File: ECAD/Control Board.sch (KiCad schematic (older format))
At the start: 74 parts, among them J3 Thermocouple, J4 SD_Card, J5 PWR/Heat, J6 FAN, J7 UPDI, Q1 IPD50N06S4L08, Q2 IPD50N06S4L08, SW1 Reflow, SW2 Stop, SW3 Set temp mode, U1 ATtiny1614-SS, U2 LD1086DT33, U3 AD8497, U4 HT16K33, U5 LM2575HVS-ADJ

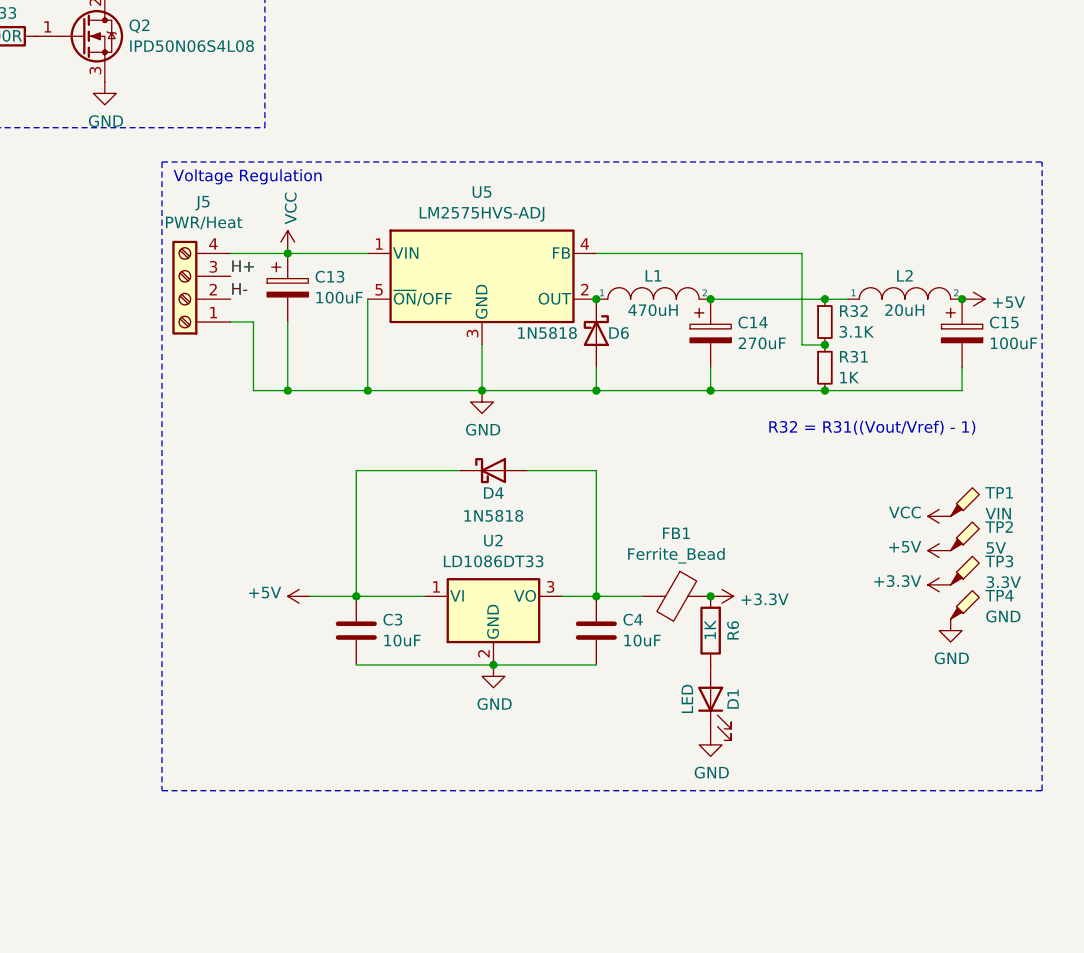
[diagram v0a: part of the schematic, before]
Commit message: Remove extra LC filter, replace with ceramic cap
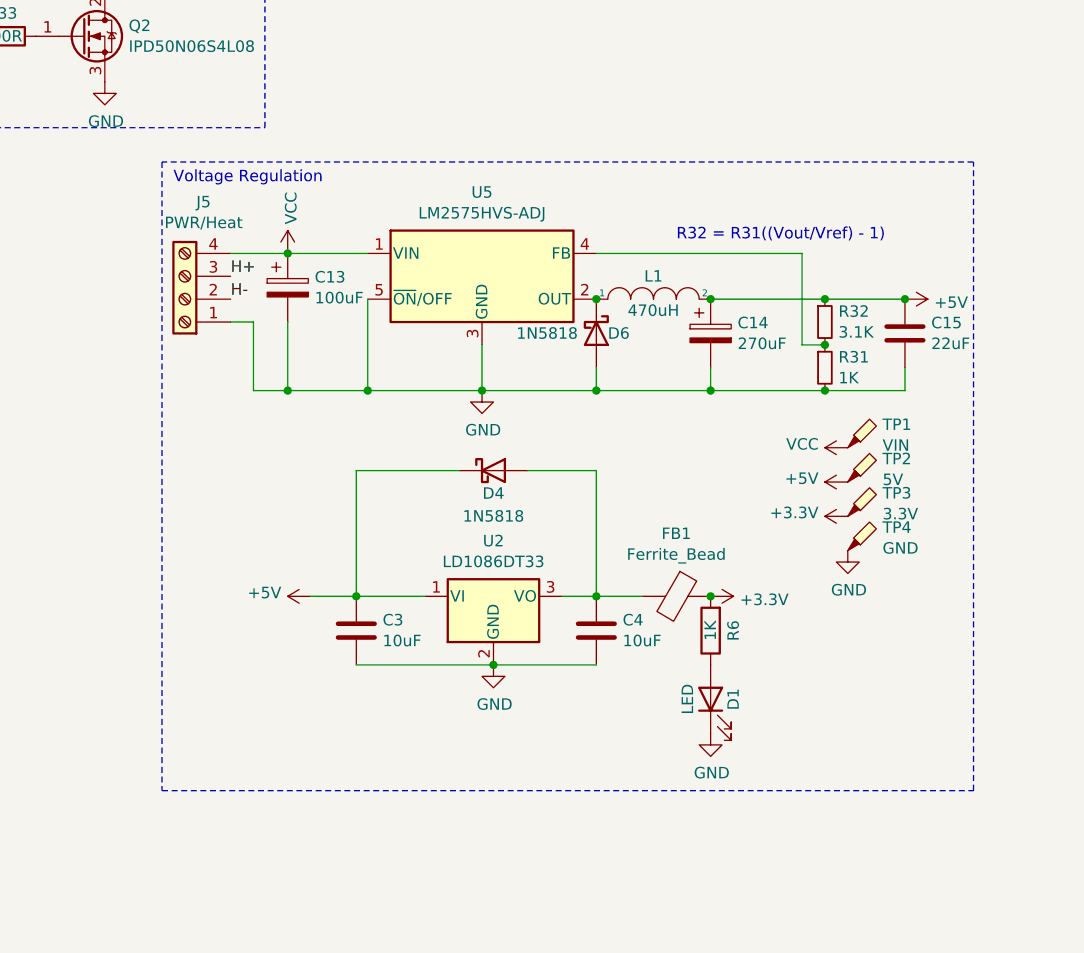
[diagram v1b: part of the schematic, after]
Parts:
- removed C15: 100uF, symbol Device:CP
- removed L2: 20uH, symbol pspice:INDUCTOR
- added C15: 22uF, Capacitor_SMD:C_0805_2012Metric_Pad1.18x1.45mm_HandSolder, symbol Device:C
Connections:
- net +5V: now also C14.1, L1.2, R32.1, C15.1
- net GND: now also C15.2
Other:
- moved on the sheet: TP1, TP2, TP3, TP4
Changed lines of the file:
@@
 	0    1    1    0
 $EndComp
-Wire Notes Line
-	7300 3700 11150 3700
-Wire Notes Line
-	7300 6450 11150 6450
-Wire Notes Line
-	11150 6450 11150 3700
 Connection ~ 10200 4300
-Wire Wire Line
-	10200 4300 10300 4300
-Connection ~ 10200 4700
-Wire Wire Line
-	10200 4700 10800 4700
 Connection ~ 9700 4700
 Connection ~ 9200 4700
@@
 Wire Wire Line
 	7600 4400 7700 4400
-Connection ~ 10800 4300
 $Comp
 L power:+5V #PWR0128
@@
 L power:+5V #PWR0129
 U 1 1 6145C041
-P 10800 4300
-F 0 "#PWR0129" H 10800 4150 50  0001 C CNN
-F 1 "+5V" V 10815 4428 50  0000 L CNN
-F 2 "" H 10800 4300 50  0001 C CNN
-F 3 "" H 10800 4300 50  0001 C CNN
-	1    10800 4300
+P 10550 4300
+F 0 "#PWR0129" H 10550 4150 50  0001 C CNN
+F 1 "+5V" V 10565 4428 50  0000 L CNN
+F 2 "" H 10550 4300 50  0001 C CNN
+F 3 "" H 10550 4300 50  0001 C CNN
+	1    10550 4300
 	0    1    1    0
 $EndComp
@@
 L power:+5V #PWR0131
 U 1 1 6145B012
-P 10750 5400
-F 0 "#PWR0131" H 10750 5250 50  0001 C CNN
-F 1 "+5V" V 10765 5528 50  0000 L CNN
-F 2 "" H 10750 5400 50  0001 C CNN
-F 3 "" H 10750 5400 50  0001 C CNN
-	1    10750 5400
+P 10300 5100
+F 0 "#PWR0131" H 10300 4950 50  0001 C CNN
+F 1 "+5V" V 10315 5228 50  0000 L CNN
+F 2 "" H 10300 5100 50  0001 C CNN
+F 3 "" H 10300 5100 50  0001 C CNN
+	1    10300 5100
 	0    -1   -1   0
 $EndComp
@@
 Wire Wire Line
 	7700 4700 7700 4400
-Wire Wire Line
-	10800 4700 10800 4600
-$Comp
-L Device:CP C15
-U 1 1 61496574
-P 10800 4450
-F 0 "C15" H 10918 4496 50  0000 L CNN
-F 1 "100uF" H 10918 4405 50  0000 L CNN
-F 2 "" H 10838 4300 50  0001 C CNN
-F 3 "~" H 10800 4450 50  0001 C CNN
-	1    10800 4450
-	1    0    0    -1
-$EndComp
-$Comp
-L pspice:INDUCTOR L2
-U 1 1 614855B5
-P 10550 4300
-F 0 "L2" H 10550 4400 50  0000 C CNN
-F 1 "20uH" H 10550 4250 50  0000 C CNN
-F 2 "" H 10550 4300 50  0001 C CNN
-F 3 "~" H 10550 4300 50  0001 C CNN
-	1    10550 4300
-	1    0    0    -1
-$EndComp
-Text Notes 9950 4900 0    50   ~ 0
+Text Notes 9550 4050 0    50   ~ 0
 R32 = R31((Vout/Vref) - 1)
 Wire Wire Line
@@
 L Connector:TestPoint_Probe TP1
 U 1 1 613AEBF8
-P 10750 5250
-F 0 "TP1" H 10902 5351 50  0000 L CNN
-F 1 "VIN" H 10902 5260 50  0000 L CNN
-F 2 "TestPoint:TestPoint_Pad_2.0x2.0mm" H 10950 5250 50  0001 C CNN
-F 3 "~" H 10950 5250 50  0001 C CNN
-	1    10750 5250
+P 10300 4950
+F 0 "TP1" H 10452 5051 50  0000 L CNN
+F 1 "VIN" H 10452 4960 50  0000 L CNN
+F 2 "TestPoint:TestPoint_Pad_2.0x2.0mm" H 10500 4950 50  0001 C CNN
+F 3 "~" H 10500 4950 50  0001 C CNN
+	1    10300 4950
 	1    0    0    -1
 $EndComp
@@
 L Connector:TestPoint_Probe TP2
 U 1 1 613AF955
-P 10750 5400
-F 0 "TP2" H 10902 5501 50  0000 L CNN
-F 1 "5V" H 10902 5410 50  0000 L CNN
-F 2 "TestPoint:TestPoint_Pad_2.0x2.0mm" H 10950 5400 50  0001 C CNN
-F 3 "~" H 10950 5400 50  0001 C CNN
-	1    10750 5400
+P 10300 5100
+F 0 "TP2" H 10452 5201 50  0000 L CNN
+F 1 "5V" H 10452 5110 50  0000 L CNN
+F 2 "TestPoint:TestPoint_Pad_2.0x2.0mm" H 10500 5100 50  0001 C CNN
+F 3 "~" H 10500 5100 50  0001 C CNN
+	1    10300 5100
 	1    0    0    -1
 $EndComp
@@
 L Connector:TestPoint_Probe TP3
 U 1 1 613B3568
-P 10750 5550
-F 0 "TP3" H 10902 5651 50  0000 L CNN
-F 1 "3.3V" H 10902 5560 50  0000 L CNN
-F 2 "TestPoint:TestPoint_Pad_2.0x2.0mm" H 10950 5550 50  0001 C CNN
-F 3 "~" H 10950 5550 50  0001 C CNN
-	1    10750 5550
+P 10300 5250
+F 0 "TP3" H 10452 5351 50  0000 L CNN
+F 1 "3.3V" H 10452 5260 50  0000 L CNN
+F 2 "TestPoint:TestPoint_Pad_2.0x2.0mm" H 10500 5250 50  0001 C CNN
+F 3 "~" H 10500 5250 50  0001 C CNN
+	1    10300 5250
 	1    0    0    -1
 $EndComp
@@
 L Connector:TestPoint_Probe TP4
 U 1 1 613B6FB0
-P 10750 5700
-F 0 "TP4" H 10902 5801 50  0000 L CNN
-F 1 "GND" H 10902 5710 50  0000 L CNN
-F 2 "TestPoint:TestPoint_Pad_2.0x2.0mm" H 10950 5700 50  0001 C CNN
-F 3 "~" H 10950 5700 50  0001 C CNN
-	1    10750 5700
+P 10300 5400
+F 0 "TP4" H 10452 5501 50  0000 L CNN
+F 1 "GND" H 10452 5410 50  0000 L CNN
+F 2 "TestPoint:TestPoint_Pad_2.0x2.0mm" H 10500 5400 50  0001 C CNN
+F 3 "~" H 10500 5400 50  0001 C CNN
+	1    10300 5400
 	1    0    0    -1
 $EndComp
@@
 L power:VCC #PWR0130
 U 1 1 613C04FB
-P 10750 5250
-F 0 "#PWR0130" H 10750 5100 50  0001 C CNN
-F 1 "VCC" V 10765 5377 50  0000 L CNN
-F 2 "" H 10750 5250 50  0001 C CNN
-F 3 "" H 10750 5250 50  0001 C CNN
-	1    10750 5250
+P 10300 4950
+F 0 "#PWR0130" H 10300 4800 50  0001 C CNN
+F 1 "VCC" V 10315 5077 50  0000 L CNN
+F 2 "" H 10300 4950 50  0001 C CNN
+F 3 "" H 10300 4950 50  0001 C CNN
+	1    10300 4950
 	0    -1   -1   0
 $EndComp
@@
 L power:+3.3V #PWR0132
 U 1 1 613C3110
-P 10750 5550
-F 0 "#PWR0132" H 10750 5400 50  0001 C CNN
-F 1 "+3.3V" V 10765 5678 50  0000 L CNN
-F 2 "" H 10750 5550 50  0001 C CNN
-F 3 "" H 10750 5550 50  0001 C CNN
-	1    10750 5550
+P 10300 5250
+F 0 "#PWR0132" H 10300 5100 50  0001 C CNN
+F 1 "+3.3V" V 10315 5378 50  0000 L CNN
+F 2 "" H 10300 5250 50  0001 C CNN
+F 3 "" H 10300 5250 50  0001 C CNN
+	1    10300 5250
 	0    -1   -1   0
 $EndComp
@@
 L power:GND #PWR0133
 U 1 1 613C7315
-P 10750 5700
-F 0 "#PWR0133" H 10750 5450 50  0001 C CNN
-F 1 "GND" H 10755 5527 50  0000 C CNN
-F 2 "" H 10750 5700 50  0001 C CNN
-F 3 "" H 10750 5700 50  0001 C CNN
-	1    10750 5700
+P 10300 5400
+F 0 "#PWR0133" H 10300 5150 50  0001 C CNN
+F 1 "GND" H 10305 5227 50  0000 C CNN
+F 2 "" H 10300 5400 50  0001 C CNN
+F 3 "" H 10300 5400 50  0001 C CNN
+	1    10300 5400
 	1    0    0    -1
 $EndComp
@@
 	1    0    0    -1
 $EndComp
+$Comp
+L Device:C C15
+U 1 1 6141E1A6
+P 10550 4450
+F 0 "C15" H 10665 4496 50  0000 L CNN
+F 1 "22uF" H 10665 4405 50  0000 L CNN
+F 2 "Capacitor_SMD:C_0805_2012Metric_Pad1.18x1.45mm_HandSolder" H 10588 4300 50  0001 C CNN
+F 3 "~" H 10550 4450 50  0001 C CNN
+	1    10550 4450
+	1    0    0    -1
+$EndComp
+Wire Wire Line
+	10550 4600 10550 4700
+Wire Wire Line
+	10550 4700 10200 4700
+Connection ~ 10200 4700
+Wire Wire Line
+	10200 4300 10550 4300
+Connection ~ 10550 4300
+Wire Notes Line
+	7300 6450 10850 6450
+Wire Notes Line
+	10850 6450 10850 3700
+Wire Notes Line
+	10850 3700 7300 3700
 $EndSCHEMATC

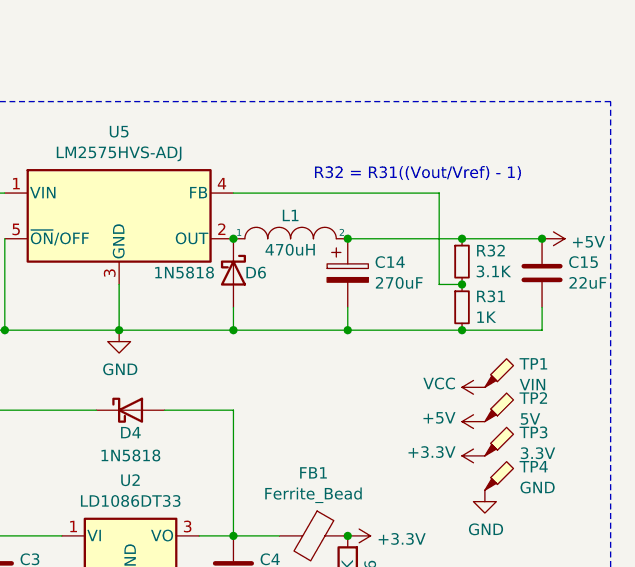
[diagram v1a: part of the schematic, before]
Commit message: Associate footprints and update board
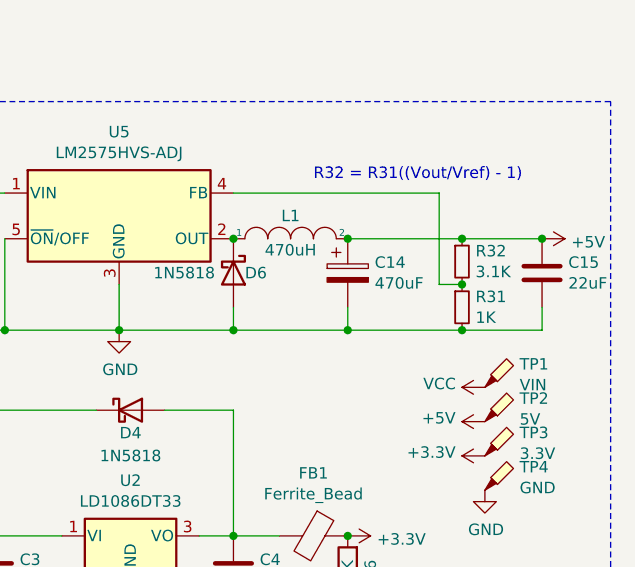
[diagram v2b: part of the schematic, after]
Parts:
- C13: footprint (none) -> Capacitor_SMD:CP_Elec_10x10.5
- C14: value 270uF -> 470uF; footprint (none) -> Capacitor_SMD:CP_Elec_8x10.5
- L1: footprint (none) -> Inductor_SMD:L_12x12mm_H8mm
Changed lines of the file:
@@
 P 9700 4450
 F 0 "C14" H 9818 4496 50  0000 L CNN
-F 1 "270uF" H 9818 4405 50  0000 L CNN
-F 2 "" H 9738 4300 50  0001 C CNN
+F 1 "470uF" H 9818 4405 50  0000 L CNN
+F 2 "Capacitor_SMD:CP_Elec_8x10.5" H 9738 4300 50  0001 C CNN
 F 3 "~" H 9700 4450 50  0001 C CNN
 	1    9700 4450
@@
 F 0 "L1" H 9450 4400 50  0000 C CNN
 F 1 "470uH" H 9450 4250 50  0000 C CNN
-F 2 "" H 9450 4300 50  0001 C CNN
+F 2 "Inductor_SMD:L_12x12mm_H8mm" H 9450 4300 50  0001 C CNN
 F 3 "~" H 9450 4300 50  0001 C CNN
 	1    9450 4300
@@
 F 0 "C13" H 7968 4296 50  0000 L CNN
 F 1 "100uF" H 7968 4205 50  0000 L CNN
-F 2 "" H 7888 4100 50  0001 C CNN
+F 2 "Capacitor_SMD:CP_Elec_10x10.5" H 7888 4100 50  0001 C CNN
 F 3 "~" H 7850 4250 50  0001 C CNN
 	1    7850 4250

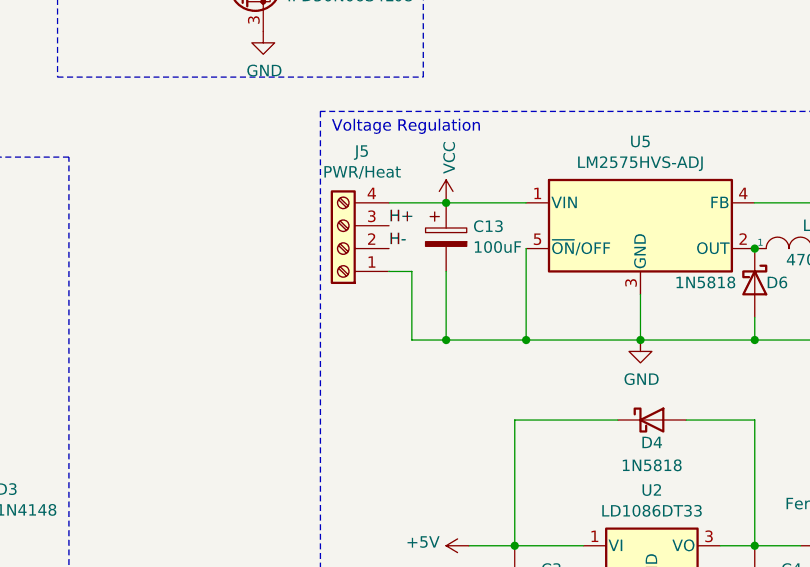
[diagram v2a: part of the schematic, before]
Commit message: Lay out switching regulator
Also reshuffling the SD card and power port placements
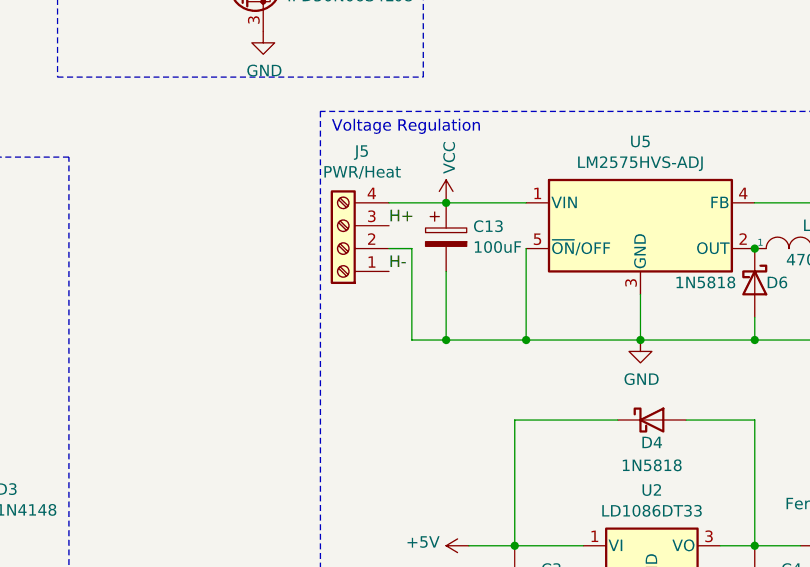
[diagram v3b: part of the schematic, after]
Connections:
- net GND: now also J5.2 (Pin_2); no longer J5.1 (Pin_1)
- net H-: now also J5.1 (Pin_1); no longer J5.2 (Pin_2)
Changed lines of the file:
@@
 Wire Wire Line
 	7600 4100 7850 4100
-Wire Wire Line
-	7600 4400 7700 4400
 $Comp
 L power:+5V #PWR0128
@@
 Wire Wire Line
 	8700 4700 9200 4700
-Wire Wire Line
-	7700 4700 7700 4400
 Text Notes 9550 4050 0    50   ~ 0
 R32 = R31((Vout/Vref) - 1)
@@
 	1    0    0    -1
 $EndComp
-Text Label 7600 4300 0    50   ~ 0
+Text Label 7600 4400 0    50   ~ 0
 H-
 Text Label 7600 4200 0    50   ~ 0
@@
 Wire Notes Line
 	10850 3700 7300 3700
+Wire Wire Line
+	7600 4300 7700 4300
+Wire Wire Line
+	7700 4300 7700 4700
 $EndSCHEMATC

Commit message: start fixing errors in board
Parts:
- removed U2: LD1086DT33, Package_TO_SOT_SMD:TO-252-3_TabPin2, symbol Regulator_Linear:LD39150DT33
- added U2: LD1086DT33, Package_TO_SOT_SMD:TO-252-3_TabPin2, symbol Regulator_Linear:IFX27001TFV33
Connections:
- net +5V: now also U2.3 (I)
- net GND: now also U2.1 (GND)
- net at C4.1, D4.2 (A), FB1.2: now also U2.2 (Q)
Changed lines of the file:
@@
-	1    0    0    -1
-$EndComp
-$Comp
-L Regulator_Linear:LD39150DT33 U2
-U 1 1 61260A04
-P 8750 5600
-F 0 "U2" H 8750 5842 50  0000 C CNN
-F 1 "LD1086DT33" H 8750 5751 50  0000 C CNN
-F 2 "Package_TO_SOT_SMD:TO-252-3_TabPin2" H 8750 5800 50  0001 C CNN
-F 3 "https://www.st.com/resource/en/datasheet/ld39150.pdf" H 8850 5350 50  0001 C CNN
-	1    8750 5600
 	1    0    0    -1
 $EndComp
@@
 Wire Wire Line
 	7700 4300 7700 4700
+$Comp
+L Regulator_Linear:IFX27001TFV33 U2
+U 1 1 61608C34
+P 8750 5600
+F 0 "U2" H 8750 5867 50  0000 C CNN
+F 1 "LD1086DT33" H 8750 5776 50  0000 C CNN
+F 2 "Package_TO_SOT_SMD:TO-252-3_TabPin2" H 8750 5550 50  0001 C CNN
+F 3 "https://static6.arrow.com/aropdfconversion/dc75757ae45a88e5f69bdce3f2a651a5fe0ca07d/ifx27001_ds_10.pdf" H 8750 5550 50  0001 C CNN
+	1    8750 5600
+	1    0    0    -1
+$EndComp
 $EndSCHEMATC

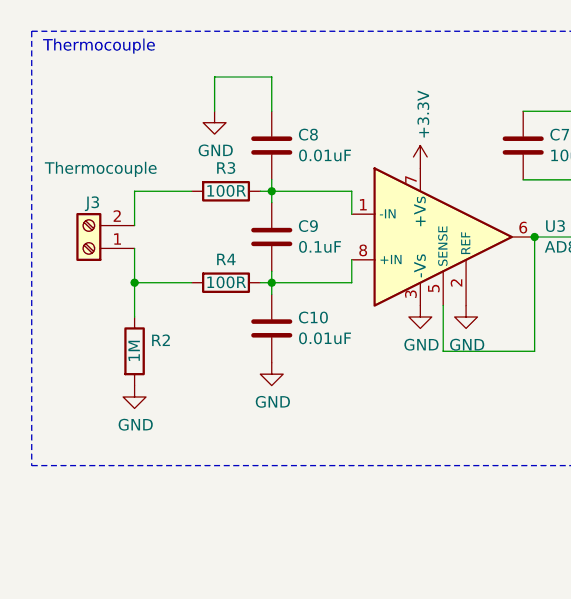
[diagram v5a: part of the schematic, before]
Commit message: Fix thermocouple + and - pins
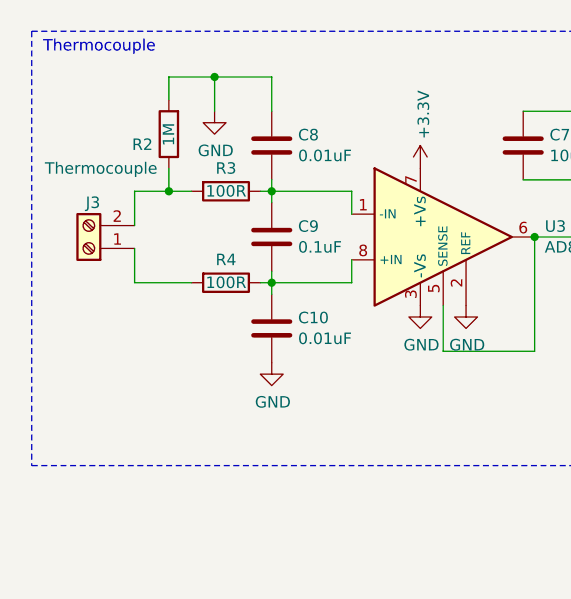
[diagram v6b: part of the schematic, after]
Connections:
- net at J3.1 (Pin_1), R4.2: no longer R2.1
- net at J3.2 (Pin_2), R3.2: now also R2.1
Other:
- moved on the sheet: R2
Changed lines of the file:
@@
 L Device:R R2
 U 1 1 6122089B
-P 950 1900
-F 0 "R2" H 1020 1946 50  0000 L CNN
-F 1 "1M" V 950 1850 50  0000 L CNN
-F 2 "Resistor_SMD:R_1206_3216Metric_Pad1.30x1.75mm_HandSolder" V 880 1900 50  0001 C CNN
-F 3 "~" H 950 1900 50  0001 C CNN
-	1    950  1900
-	1    0    0    -1
-$EndComp
-$Comp
-L power:GND #PWR0107
-U 1 1 6122286B
-P 950 2050
-F 0 "#PWR0107" H 950 1800 50  0001 C CNN
-F 1 "GND" H 955 1877 50  0000 C CNN
-F 2 "" H 950 2050 50  0001 C CNN
-F 3 "" H 950 2050 50  0001 C CNN
-	1    950  2050
-	1    0    0    -1
+P 1100 950
+F 0 "R2" H 1170 996 50  0000 L CNN
+F 1 "1M" V 1100 900 50  0000 L CNN
+F 2 "Resistor_SMD:R_1206_3216Metric_Pad1.30x1.75mm_HandSolder" V 1030 950 50  0001 C CNN
+F 3 "~" H 1100 950 50  0001 C CNN
+	1    1100 950
+	-1   0    0    1
 $EndComp
 Wire Wire Line
@@
 Wire Wire Line
 	950  1600 1200 1600
-Connection ~ 950  1600
-Wire Wire Line
-	950  1600 950  1750
 $Comp
 L Device:R R4
@@
 	950  1350 950  1200
 Wire Wire Line
-	950  1200 1200 1200
+	950  1200 1100 1200
 $Comp
 L Device:C C9
@@
 	1    0    0    -1
 $EndComp
+Wire Wire Line
+	1300 700  1100 700
+Wire Wire Line
+	1100 700  1100 800
+Connection ~ 1300 700
+Wire Wire Line
+	1100 1100 1100 1200
+Connection ~ 1100 1200
+Wire Wire Line
+	1100 1200 1200 1200
 $EndSCHEMATC
